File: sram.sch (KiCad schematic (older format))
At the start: 1 part

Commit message: Made a overview on the toplevel schematic and added the SRAM subschematic.
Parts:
- removed U?: IS61C5128AS-25TLI, Package_SO:TSOP-II-32_21.0x10.2mm_P1.27mm, symbol Memory_RAM:IS61C5128AS-25TLI
- added U1: ICE40HX4K-TQ144, symbol ice40hx4k:ICE40HX4K-TQ144
- added U2: IS62WV5128EBLL-45HLI, Package_SO:TSOP-I-32_18.4x8mm_P0.5mm, symbol IS62WV5128:IS62WV5128EBLL-45HLI
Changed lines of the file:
@@
 EESchema Schematic File Version 4
+LIBS:ice40_breakout-cache
 EELAYER 29 0
 EELAYER END
 $Descr A4 11693 8268
 encoding utf-8
-Sheet 5 5
+Sheet 4 6
 Title ""
 Date ""
@@
 $EndDescr
 $Comp
-L Memory_RAM:IS61C5128AS-25TLI U?
-U 1 1 5CAE0A70
-P 8650 2775
-F 0 "U?" H 8650 4256 50  0000 C CNN
-F 1 "IS61C5128AS-25TLI" H 8650 4165 50  0000 C CNN
-F 2 "Package_SO:TSOP-II-32_21.0x10.2mm_P1.27mm" H 8150 3925 50  0001 C CNN
-F 3 "http://www.issi.com/WW/pdf/61-64C5128AL.pdf" H 8650 2775 50  0001 C CNN
-	1    8650 2775
+L IS62WV5128:IS62WV5128EBLL-45HLI U2
+U 1 1 5CAAC6E3
+P 8600 4200
+F 0 "U2" H 8000 2900 50  0000 C CNN
+F 1 "IS62WV5128EBLL-45HLI" H 8775 5475 50  0000 C CNN
+F 2 "Package_SO:TSOP-I-32_18.4x8mm_P0.5mm" H 8500 2300 50  0001 C CNN
+F 3 "http://www.issi.com/WW/pdf/62-65WV5128EALL-BLL.pdf" H 8850 4550 50  0001 C CNN
+	1    8600 4200
 	1    0    0    -1
 $EndComp
+$Comp
+L ice40hx4k:ICE40HX4K-TQ144 U1
+U 3 1 5CABA9E6
+P 3425 3650
+F 0 "U1" H 4403 3849 50  0000 L CNN
+F 1 "ICE40HX4K-TQ144" H 4403 3758 50  0000 L CNN
+F 2 "" H 3425 3650 50  0001 C CNN
+F 3 "" H 3425 3650 50  0001 C CNN
+	3    3425 3650
+	1    0    0    -1
+$EndComp

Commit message: sram, ui, power, flash and header
SRAM: mostly done. Changed the choosen IC to a faster one in a differenc housing.

POWER: added some step down converter for 3.3 V and 1.2 V. The 1.2 V is oversized and could be changed to a smaller one

Programmer: added flash.

HEADER: Added Arduino Uno like headers with 5 V signal level. Analog is not connected now, will get an I2C ADC in future. Also added 3 digilent pmod styled connector with 3.3 V signal level.

UI: added 5 buttons and 8 LEDs. There is some space left over, maybe double the LED count in future.
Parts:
- removed U2: IS62WV5128EBLL-45HLI, Package_SO:TSOP-I-32_18.4x8mm_P0.5mm, symbol IS62WV5128:IS62WV5128EBLL-45HLI
- added U2: IS61WV5128EDBLL-10TLI, Package_SO:TSOP-II-44_10.16x18.41mm_P0.8mm, symbol is61wv5128edbll:IS61WV5128EDBLL-10TLI
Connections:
- net labels added: A0, A1, A10, A11, A12, A13, A14, A15, A16, A17, A18, A2, A3, A4, A5, A6, A7, A8, A9, IO0, IO1, IO2, IO3, IO4, IO5, IO6, IO7, ~SRAM_CE~, ~SRAM_OE~, ~SRAM_WE~
- wire segments 0 -> 59

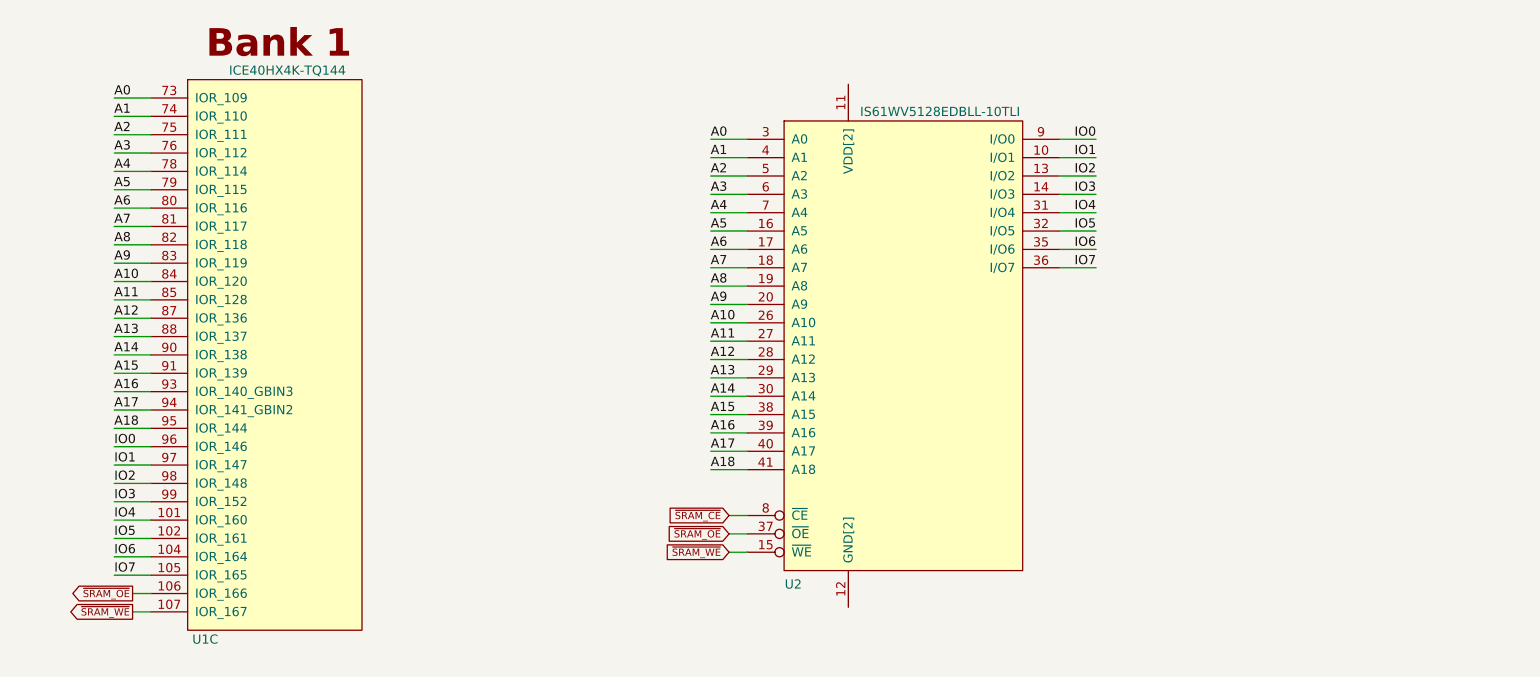
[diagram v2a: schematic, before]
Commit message: Continued on Programmer, moved the header signals around the package to free some space for a fully featured UART/RS232(TTL)
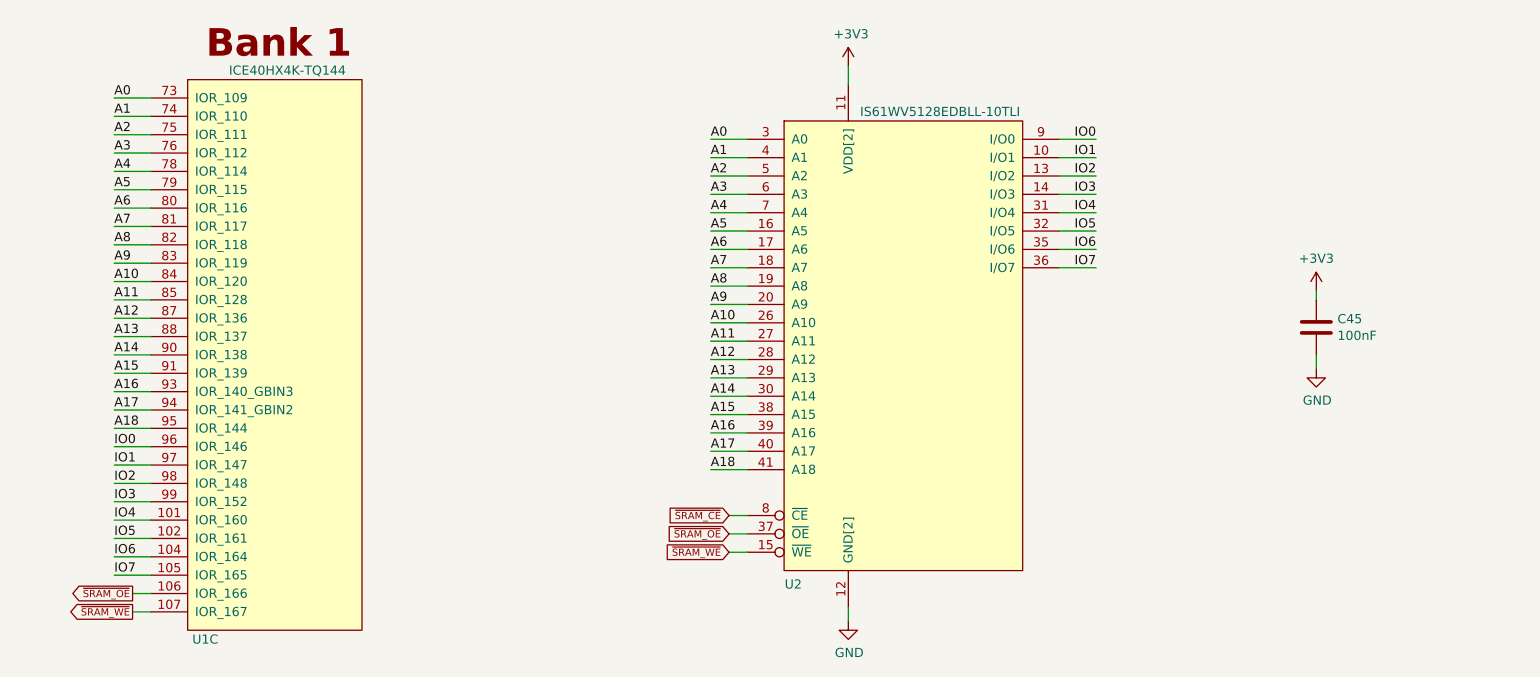
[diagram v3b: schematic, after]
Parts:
- added C45: 100nF, Capacitor_SMD:C_0603_1608Metric, symbol Device:C
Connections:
- net +3V3: now reaches U2.11 (VDD[2]), U2.33 (VDD)
- net +3V3: now also C45.1
- net GND: now reaches U2.12 (GND[2]), U2.34 (GND)
- net GND: now also C45.2
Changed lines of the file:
@@
 Wire Wire Line
 	3125 5050 3225 5050
+$Comp
+L power:GND #PWR0131
+U 1 1 5D034D1A
+P 7025 5100
+F 0 "#PWR0131" H 7025 4850 50  0001 C CNN
+F 1 "GND" H 7030 4927 50  0000 C CNN
+F 2 "" H 7025 5100 50  0001 C CNN
+F 3 "" H 7025 5100 50  0001 C CNN
+	1    7025 5100
+	1    0    0    -1
+$EndComp
+Wire Wire Line
+	7025 5100 7025 5025
+$Comp
+L power:+3V3 #PWR0132
+U 1 1 5D037261
+P 7025 2075
+F 0 "#PWR0132" H 7025 1925 50  0001 C CNN
+F 1 "+3V3" H 7040 2248 50  0000 C CNN
+F 2 "" H 7025 2075 50  0001 C CNN
+F 3 "" H 7025 2075 50  0001 C CNN
+	1    7025 2075
+	1    0    0    -1
+$EndComp
+Wire Wire Line
+	7025 2075 7025 2175
+$Comp
+L power:+3V3 #PWR?
+U 1 1 5D1D0369
+P 9575 3300
+AR Path="/5CAB8B22/5D1D0369" Ref="#PWR?"  Part="1"
+AR Path="/5CADFC7F/5D1D0369" Ref="#PWR0133"  Part="1"
+F 0 "#PWR0133" H 9575 3150 50  0001 C CNN
+F 1 "+3V3" H 9575 3475 50  0000 C CNN
+F 2 "" H 9575 3300 50  0001 C CNN
+F 3 "" H 9575 3300 50  0001 C CNN
+	1    9575 3300
+	1    0    0    -1
+$EndComp
+$Comp
+L power:GND #PWR?
+U 1 1 5D1D036F
+P 9575 3725
+AR Path="/5CAB8B22/5D1D036F" Ref="#PWR?"  Part="1"
+AR Path="/5CADFC7F/5D1D036F" Ref="#PWR0134"  Part="1"
+F 0 "#PWR0134" H 9575 3475 50  0001 C CNN
+F 1 "GND" H 9580 3552 50  0000 C CNN
+F 2 "" H 9575 3725 50  0001 C CNN
+F 3 "" H 9575 3725 50  0001 C CNN
+	1    9575 3725
+	1    0    0    -1
+$EndComp
+Wire Wire Line
+	9575 3725 9575 3650
+Wire Wire Line
+	9575 3350 9575 3300
+$Comp
+L Device:C C?
+U 1 1 5D2D1DCF
+P 9575 3500
+AR Path="/5CAB7CD4/5D2D1DCF" Ref="C?"  Part="1"
+AR Path="/5CB5889B/5D2D1DCF" Ref="C?"  Part="1"
+AR Path="/5CADFC7F/5D2D1DCF" Ref="C45"  Part="1"
+F 0 "C45" H 9690 3546 50  0000 L CNN
+F 1 "100nF" H 9690 3455 50  0000 L CNN
+F 2 "Capacitor_SMD:C_0603_1608Metric" H 9613 3350 50  0001 C CNN
+F 3 "~" H 9575 3500 50  0001 C CNN
+	1    9575 3500
+	1    0    0    -1
+$EndComp
 $EndSCHEMATC

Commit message: Continued with routing
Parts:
- added C85: 100nF, Capacitor_SMD:C_0603_1608Metric, symbol Device:C
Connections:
- net +3V3: now also C85.1
- net A10: now also U1.101 (IOR_160); no longer U1.84 (IOR_120)
- net A11: now also U1.99 (IOR_152); no longer U1.85 (IOR_128)
- net A12: now also U1.98 (IOR_148); no longer U1.87 (IOR_136)
- net A13: now also U1.97 (IOR_147); no longer U1.88 (IOR_137)
- net A14: now also U1.96 (IOR_146); no longer U1.90 (IOR_138)
- net A15: now also U1.85 (IOR_128); no longer U1.91 (IOR_139)
- net A16: now also U1.83 (IOR_119); no longer U1.93 (IOR_140_GBIN3)
- net A17: now also U1.81 (IOR_117); no longer U1.94 (IOR_141_GBIN2)
- net A18: now also U1.79 (IOR_115); no longer U1.95 (IOR_144)
- net A5: now also U1.102 (IOR_161); no longer U1.79 (IOR_115)
- net A6: now also U1.104 (IOR_164); no longer U1.80 (IOR_116)
- net A7: now also U1.105 (IOR_165); no longer U1.81 (IOR_117)
- net A8: now also U1.106 (IOR_166); no longer U1.82 (IOR_118)
- net A9: now also U1.107 (IOR_167); no longer U1.83 (IOR_119)
- net GND: now also C85.2
- net IO0: now also U1.80 (IOR_116); no longer U1.96 (IOR_146)
- net IO1: now also U1.82 (IOR_118); no longer U1.97 (IOR_147)
- net IO2: now also U1.84 (IOR_120); no longer U1.98 (IOR_148)
- net IO3: now also U1.91 (IOR_139); no longer U1.99 (IOR_152)
- net IO4: now also U1.95 (IOR_144); no longer U1.101 (IOR_160)
- net IO5: now also U1.93 (IOR_140_GBIN3); no longer U1.102 (IOR_161)
- net IO6: now also U1.90 (IOR_138); no longer U1.104 (IOR_164)
- net IO7: now also U1.88 (IOR_137); no longer U1.105 (IOR_165)
- net ~SRAM_OE~: now also U1.87 (IOR_136); no longer U1.106 (IOR_166)
- net ~SRAM_WE~: now also U1.94 (IOR_141_GBIN2); no longer U1.107 (IOR_167)
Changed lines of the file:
@@
 Wire Wire Line
 	3025 2650 3225 2650
+Text Label 3025 4650 0    50   ~ 0
+A5
+Wire Wire Line
+	3025 4650 3225 4650
+Text Label 3025 4750 0    50   ~ 0
+A6
+Wire Wire Line
+	3025 4750 3225 4750
+Text Label 3025 4850 0    50   ~ 0
+A7
+Wire Wire Line
+	3025 4850 3225 4850
+Text Label 3025 4950 0    50   ~ 0
+A8
+Wire Wire Line
+	3025 4950 3225 4950
+Text Label 3025 5050 0    50   ~ 0
+A9
+Wire Wire Line
+	3025 5050 3225 5050
+Text Label 3025 4550 0    50   ~ 0
+A10
+Wire Wire Line
+	3025 4550 3225 4550
+Text Label 3025 4450 0    50   ~ 0
+A11
+Wire Wire Line
+	3025 4450 3225 4450
+Text Label 3025 4350 0    50   ~ 0
+A12
+Wire Wire Line
+	3025 4350 3225 4350
+Text Label 3025 4250 0    50   ~ 0
+A13
+Wire Wire Line
+	3025 4250 3225 4250
+Text Label 3025 4150 0    50   ~ 0
+A14
+Wire Wire Line
+	3025 4150 3225 4150
+Text Label 3025 3350 0    50   ~ 0
+A15
+Wire Wire Line
+	3025 3350 3225 3350
+Text Label 3025 3150 0    50   ~ 0
+A16
+Wire Wire Line
+	3025 3150 3225 3150
+Text Label 3025 2950 0    50   ~ 0
+A17
+Wire Wire Line
+	3025 2950 3225 2950
 Text Label 3025 2750 0    50   ~ 0
-A5
+A18
 Wire Wire Line
 	3025 2750 3225 2750
-Text Label 3025 2850 0    50   ~ 0
-A6
-Wire Wire Line
-	3025 2850 3225 2850
-Text Label 3025 2950 0    50   ~ 0
-A7
-Wire Wire Line
-	3025 2950 3225 2950
-Text Label 3025 3050 0    50   ~ 0
-A8
-Wire Wire Line
-	3025 3050 3225 3050
-Text Label 3025 3150 0    50   ~ 0
-A9
-Wire Wire Line
-	3025 3150 3225 3150
-Text Label 3025 3250 0    50   ~ 0
-A10
-Wire Wire Line
-	3025 3250 3225 3250
-Text Label 3025 3350 0    50   ~ 0
-A11
-Wire Wire Line
-	3025 3350 3225 3350
-Text Label 3025 3450 0    50   ~ 0
-A12
-Wire Wire Line
-	3025 3450 3225 3450
-Text Label 3025 3550 0    50   ~ 0
-A13
-Wire Wire Line
-	3025 3550 3225 3550
-Text Label 3025 3650 0    50   ~ 0
-A14
-Wire Wire Line
-	3025 3650 3225 3650
-Text Label 3025 3750 0    50   ~ 0
-A15
-Wire Wire Line
-	3025 3750 3225 3750
-Text Label 3025 3850 0    50   ~ 0
-A16
-Wire Wire Line
-	3025 3850 3225 3850
-Text Label 3025 3950 0    50   ~ 0
-A17
-Wire Wire Line
-	3025 3950 3225 3950
-Text Label 3025 4050 0    50   ~ 0
-A18
-Wire Wire Line
-	3025 4050 3225 4050
 Text Label 8375 2475 2    50   ~ 0
 IO0
@@
 Wire Wire Line
 	8375 3175 8175 3175
-Text Label 3025 4150 0    50   ~ 0
+Text Label 3025 2850 0    50   ~ 0
 IO0
 Wire Wire Line
-	3025 4150 3225 4150
-Text Label 3025 4250 0    50   ~ 0
-IO1
-Wire Wire Line
-	3025 4250 3225 4250
-Text Label 3025 4350 0    50   ~ 0
-IO2
-Wire Wire Line
-	3025 4350 3225 4350
-Text Label 3025 4450 0    50   ~ 0
+	3025 2850 3225 2850
+Text Label 3025 3750 0    50   ~ 0
 IO3
 Wire Wire Line
-	3025 4450 3225 4450
-Text Label 3025 4550 0    50   ~ 0
+	3025 3750 3225 3750
+Text Label 3025 4050 0    50   ~ 0
 IO4
 Wire Wire Line
-	3025 4550 3225 4550
-Text Label 3025 4650 0    50   ~ 0
-IO5
-Wire Wire Line
-	3025 4650 3225 4650
-Text Label 3025 4750 0    50   ~ 0
+	3025 4050 3225 4050
+Text Label 3025 3650 0    50   ~ 0
 IO6
 Wire Wire Line
-	3025 4750 3225 4750
-Text Label 3025 4850 0    50   ~ 0
+	3025 3650 3225 3650
+Text Label 3025 3550 0    50   ~ 0
 IO7
 Wire Wire Line
-	3025 4850 3225 4850
+	3025 3550 3225 3550
 Text GLabel 6375 4525 0    39   Input ~ 0
 ~SRAM_CE~
@@
 Wire Wire Line
 	6375 4725 6475 4725
-Text GLabel 3125 4950 0    39   Output ~ 0
+Text GLabel 3000 3450 0    39   Output ~ 0
 ~SRAM_OE~
 Wire Wire Line
-	3125 4950 3225 4950
-Text GLabel 3125 5050 0    39   Output ~ 0
-~SRAM_WE~
-Wire Wire Line
-	3125 5050 3225 5050
+	3000 3450 3225 3450
 $Comp
 L power:GND #PWR0131
@@
 	1    0    0    -1
 $EndComp
+$Comp
+L power:+3V3 #PWR?
+U 1 1 6172BD60
+P 10050 3300
+AR Path="/5CAB8B22/6172BD60" Ref="#PWR?"  Part="1"
+AR Path="/5CADFC7F/6172BD60" Ref="#PWR0190"  Part="1"
+F 0 "#PWR0190" H 10050 3150 50  0001 C CNN
+F 1 "+3V3" H 10050 3475 50  0000 C CNN
+F 2 "" H 10050 3300 50  0001 C CNN
+F 3 "" H 10050 3300 50  0001 C CNN
+	1    10050 3300
+	1    0    0    -1
+$EndComp
+$Comp
+L power:GND #PWR?
+U 1 1 6172BD6A
+P 10050 3725
+AR Path="/5CAB8B22/6172BD6A" Ref="#PWR?"  Part="1"
+AR Path="/5CADFC7F/6172BD6A" Ref="#PWR0191"  Part="1"
+F 0 "#PWR0191" H 10050 3475 50  0001 C CNN
+F 1 "GND" H 10055 3552 50  0000 C CNN
+F 2 "" H 10050 3725 50  0001 C CNN
+F 3 "" H 10050 3725 50  0001 C CNN
+	1    10050 3725
+	1    0    0    -1
+$EndComp
+Wire Wire Line
+	10050 3725 10050 3650
+Wire Wire Line
+	10050 3350 10050 3300
+$Comp
+L Device:C C?
+U 1 1 6172BD76
+P 10050 3500
+AR Path="/5CAB7CD4/6172BD76" Ref="C?"  Part="1"
+AR Path="/5CB5889B/6172BD76" Ref="C?"  Part="1"
+AR Path="/5CADFC7F/6172BD76" Ref="C85"  Part="1"
+F 0 "C85" H 10165 3546 50  0000 L CNN
+F 1 "100nF" H 10165 3455 50  0000 L CNN
+F 2 "Capacitor_SMD:C_0603_1608Metric" H 10088 3350 50  0001 C CNN
+F 3 "~" H 10050 3500 50  0001 C CNN
+	1    10050 3500
+	1    0    0    -1
+$EndComp
+Wire Wire Line
+	3025 3250 3225 3250
+Wire Wire Line
+	3000 3950 3225 3950
+Text GLabel 3000 3950 0    39   Output ~ 0
+~SRAM_WE~
+Wire Wire Line
+	3025 3050 3225 3050
+Text Label 3025 3050 0    50   ~ 0
+IO1
+Text Label 3025 3250 0    50   ~ 0
+IO2
+Wire Wire Line
+	3025 3850 3225 3850
+Text Label 3025 3850 0    50   ~ 0
+IO5
 $EndSCHEMATC

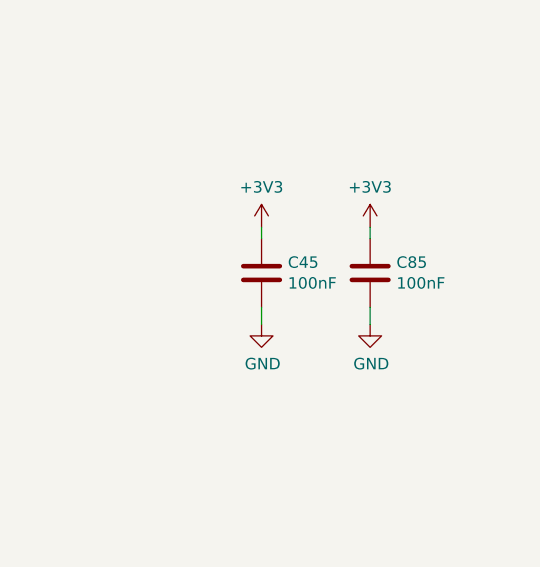
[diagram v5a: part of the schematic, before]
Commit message: Added more BOM information, updated fpga symbol, added some more 3d models
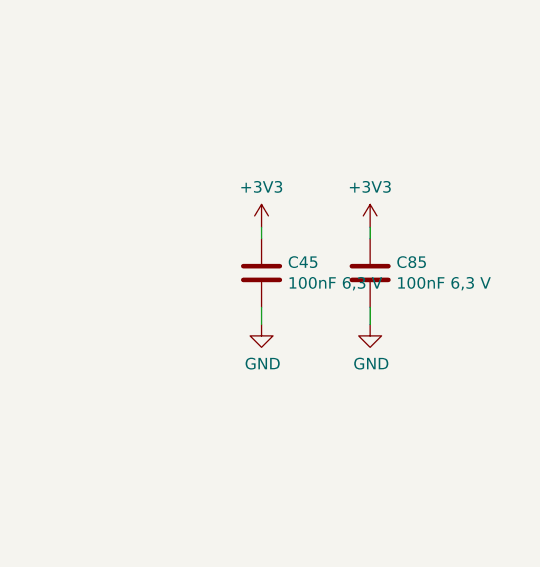
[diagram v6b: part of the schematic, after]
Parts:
- C45, C85: value 100nF -> 100nF 6,3 V; Description (none) -> CAP CER 0.1UF 50V X7R 0603; Digikey (none) -> 1276-1000-1-ND; Mfg Name (none) -> Samsung Electro-Mechanics; Mfg Part Num (none) -> CL10B104KB8NNNC; Spec (none) -> Any
- U1: Description (none) -> IC FPGA 107 I/O 144TQFP; Digikey (none) -> 220-1572-ND; Mfg Name (none) -> Lattice Semiconductor Corporation; Mfg Part Num (none) -> ICE40HX4K-TQ144; Spec (none) -> Spec
- U2: Description (none) -> C SRAM 4M PARALLEL 44TSOP2; Digikey (none) -> 706-1147-ND; Mfg Name (none) -> ISSI, Integrated Silicon Solution Inc; Mfg Part Num (none) -> IS61WV5128EDBLL-10TLI; Spec (none) -> Spec
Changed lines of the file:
@@
 U 3 1 5CABA9E6
 P 3425 3650
+AR Path="/5CABA9E6" Ref="U1"  Part="3"
+AR Path="/5CADFC7F/5CABA9E6" Ref="U1"  Part="3"
 F 0 "U1" H 3450 2100 50  0000 L CNN
 F 1 "ICE40HX4K-TQ144" H 3650 5200 50  0000 L CNN
 F 2 "" H 3425 3650 50  0001 C CNN
 F 3 "" H 3425 3650 50  0001 C CNN
+F 4 "IC FPGA 107 I/O 144TQFP" H 0   0   50  0001 C CNN "Description"
+F 5 "220-1572-ND" H 0   0   50  0001 C CNN "Digikey"
+F 6 "Lattice Semiconductor Corporation" H 0   0   50  0001 C CNN "Mfg Name"
+F 7 "ICE40HX4K-TQ144" H 0   0   50  0001 C CNN "Mfg Part Num"
+F 8 "Spec" H 0   0   50  0001 C CNN "Spec"
 	3    3425 3650
 	1    0    0    -1
@@
 AR Path="/5CADFC7F/5D2D1DCF" Ref="C45"  Part="1"
 F 0 "C45" H 9690 3546 50  0000 L CNN
-F 1 "100nF" H 9690 3455 50  0000 L CNN
+F 1 "100nF 6,3 V" H 9690 3455 50  0000 L CNN
 F 2 "Capacitor_SMD:C_0603_1608Metric" H 9613 3350 50  0001 C CNN
 F 3 "~" H 9575 3500 50  0001 C CNN
+F 4 "CAP CER 0.1UF 50V X7R 0603" H 0   0   50  0001 C CNN "Description"
+F 5 "1276-1000-1-ND" H 0   0   50  0001 C CNN "Digikey"
+F 6 "Samsung Electro-Mechanics" H 0   0   50  0001 C CNN "Mfg Name"
+F 7 "CL10B104KB8NNNC" H 0   0   50  0001 C CNN "Mfg Part Num"
+F 8 "Any" H 0   0   50  0001 C CNN "Spec"
 	1    9575 3500
 	1    0    0    -1
@@
 F 2 "Package_SO:TSOP-II-44_10.16x18.41mm_P0.8mm" H 7225 1675 50  0001 C CNN
 F 3 "http://www.issi.com/WW/pdf/61-64WV5128EDBLL.pdf" H 7575 3925 50  0001 C CNN
+F 4 "C SRAM 4M PARALLEL 44TSOP2" H 0   0   50  0001 C CNN "Description"
+F 5 "706-1147-ND" H 0   0   50  0001 C CNN "Digikey"
+F 6 "ISSI, Integrated Silicon Solution Inc" H 0   0   50  0001 C CNN "Mfg Name"
+F 7 "IS61WV5128EDBLL-10TLI" H 0   0   50  0001 C CNN "Mfg Part Num"
+F 8 "Spec" H 0   0   50  0001 C CNN "Spec"
 	1    7325 3575
 	1    0    0    -1
@@
 AR Path="/5CADFC7F/6172BD76" Ref="C85"  Part="1"
 F 0 "C85" H 10165 3546 50  0000 L CNN
-F 1 "100nF" H 10165 3455 50  0000 L CNN
+F 1 "100nF 6,3 V" H 10165 3455 50  0000 L CNN
 F 2 "Capacitor_SMD:C_0603_1608Metric" H 10088 3350 50  0001 C CNN
 F 3 "~" H 10050 3500 50  0001 C CNN
+F 4 "CAP CER 0.1UF 50V X7R 0603" H 0   0   50  0001 C CNN "Description"
+F 5 "1276-1000-1-ND" H 0   0   50  0001 C CNN "Digikey"
+F 6 "Samsung Electro-Mechanics" H 0   0   50  0001 C CNN "Mfg Name"
+F 7 "CL10B104KB8NNNC" H 0   0   50  0001 C CNN "Mfg Part Num"
+F 8 "Any" H 0   0   50  0001 C CNN "Spec"
 	1    10050 3500
 	1    0    0    -1
